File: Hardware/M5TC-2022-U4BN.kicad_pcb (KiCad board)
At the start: 2 copper layers, 127 x 127 mm, 71 parts, among them J1 VCC, J10 SLIDE_DATA_0, J11 SLIDE_DATA_1, J12 SLIDE_DATA_2, J13 SLIDE_DATA_3, J14 ISP, J15 A-G, J2 GND, J3 DATA_0, J4 DATA_1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

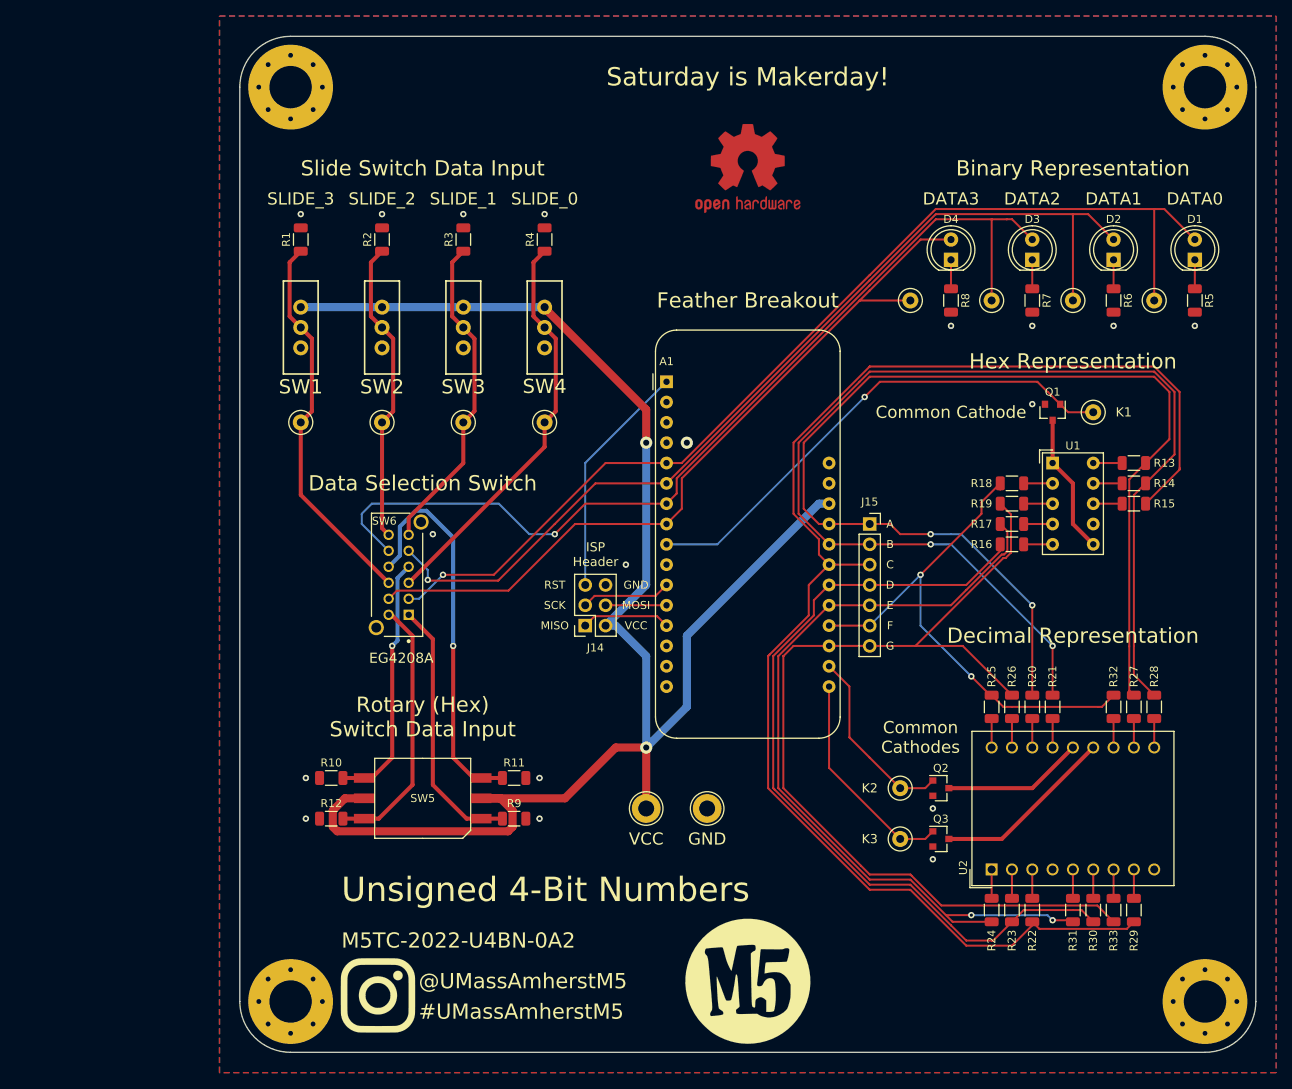
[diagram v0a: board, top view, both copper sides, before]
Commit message: Added triple test points
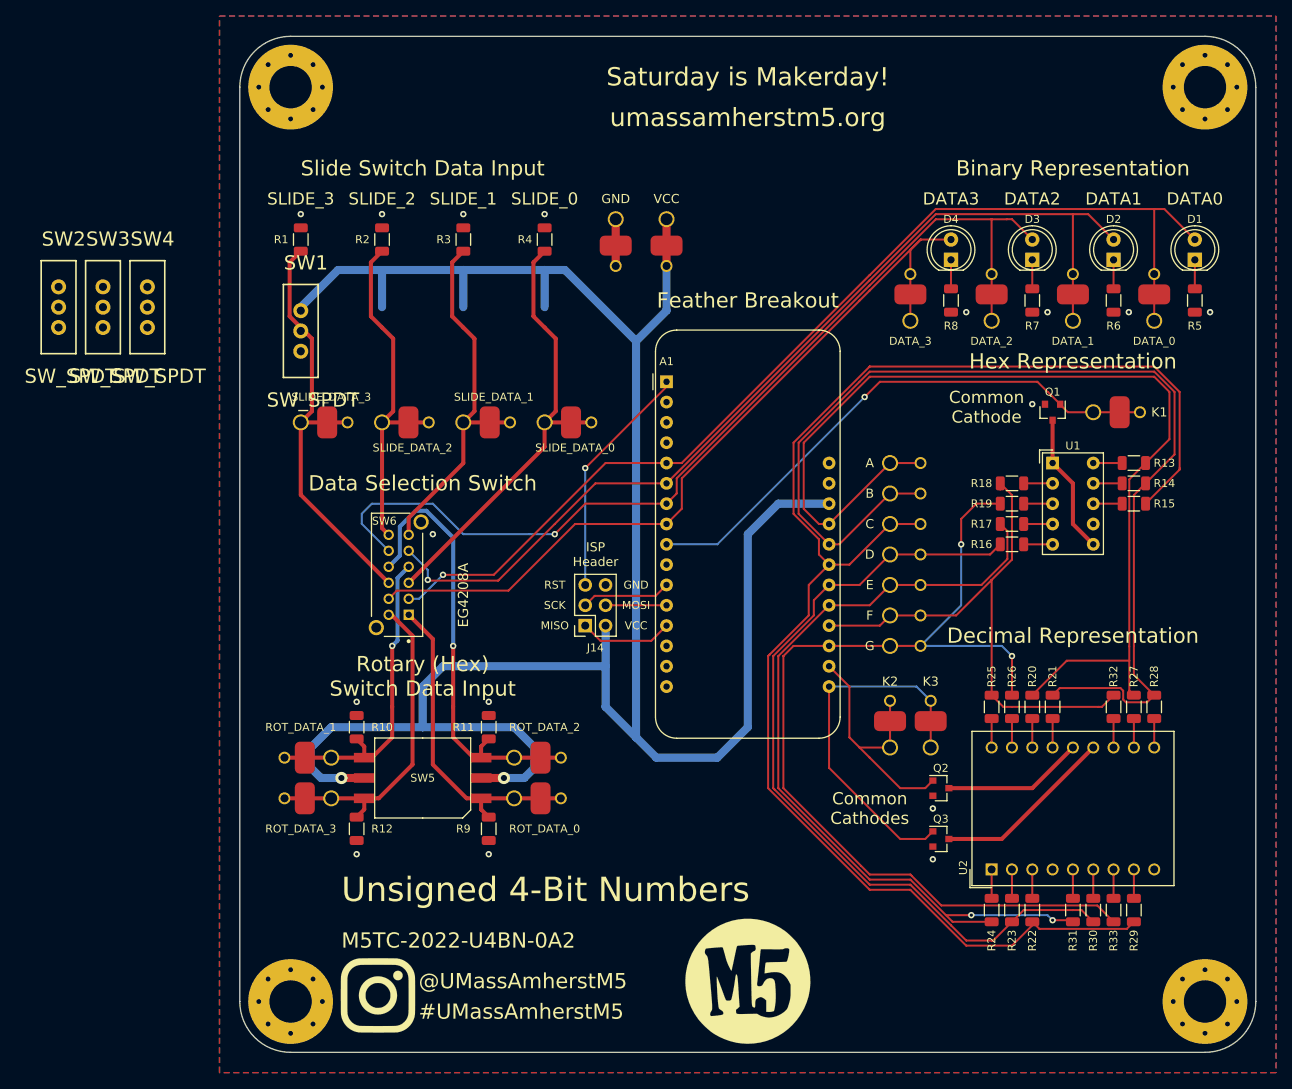
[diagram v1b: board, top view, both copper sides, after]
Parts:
- removed J1: VCC, TestPoint:TestPoint_Loop_D3.80mm_Drill2.0mm
- removed J10: SLIDE_DATA_0, TestPoint:TestPoint_Loop_D2.50mm_Drill1.0mm
- removed J11: SLIDE_DATA_1, TestPoint:TestPoint_Loop_D2.50mm_Drill1.0mm
- removed J12: SLIDE_DATA_2, TestPoint:TestPoint_Loop_D2.50mm_Drill1.0mm
- removed J13: SLIDE_DATA_3, TestPoint:TestPoint_Loop_D2.50mm_Drill1.0mm
- removed J15: A-G, Connector_PinSocket_2.54mm:PinSocket_1x07_P2.54mm_Vertical
- removed J2: GND, TestPoint:TestPoint_Loop_D3.80mm_Drill2.0mm
- removed J3: DATA_0, TestPoint:TestPoint_Loop_D2.50mm_Drill1.0mm
- removed J4: DATA_1, TestPoint:TestPoint_Loop_D2.50mm_Drill1.0mm
- removed J5: DATA_2, TestPoint:TestPoint_Loop_D2.50mm_Drill1.0mm
- removed J6: DATA_3, TestPoint:TestPoint_Loop_D2.50mm_Drill1.0mm
- removed J7: K1, TestPoint:TestPoint_Loop_D2.50mm_Drill1.0mm
- removed J8: K2, TestPoint:TestPoint_Loop_D2.50mm_Drill1.0mm
- removed J9: K3, TestPoint:TestPoint_Loop_D2.50mm_Drill1.0mm
- removed REF**: OSHW-Logo2_14.6x12mm_Copper, Symbol:OSHW-Logo2_14.6x12mm_Copper
- added TP1: VCC, Custom_TestPoint:TestPoint_LoopPostPad, F.Cu at (205.7, 124.5)
- added TP10: Conn_01x01, Custom_TestPoint:TestPoint_LoopPost, F.Cu at (233.7, 166.4)
- added TP11: Conn_01x01, Custom_TestPoint:TestPoint_LoopPost, F.Cu at (233.7, 170.2)
- added TP12: Conn_01x01, Custom_TestPoint:TestPoint_LoopPost, F.Cu at (233.7, 174.0)
- added TP13: Conn_01x01, Custom_TestPoint:TestPoint_LoopPost, F.Cu at (233.7, 177.8)
- added TP14: K1, Custom_TestPoint:TestPoint_LoopPostPad, F.Cu at (259.1, 148.6)
- added TP15: K2, Custom_TestPoint:TestPoint_LoopPostPad, F.Cu at (233.7, 190.5)
- added TP16: K3, Custom_TestPoint:TestPoint_LoopPostPad, F.Cu at (238.8, 190.5)
- added TP17: SLIDE_DATA_0, Custom_TestPoint:TestPoint_LoopPostPad, F.Cu at (190.5, 149.9)
- added TP18: SLIDE_DATA_1, Custom_TestPoint:TestPoint_LoopPostPad, F.Cu at (180.3, 149.9)
- added TP19: SLIDE_DATA_2, Custom_TestPoint:TestPoint_LoopPostPad, F.Cu at (170.2, 149.9)
- added TP2: GND, Custom_TestPoint:TestPoint_LoopPostPad, F.Cu at (199.4, 124.5)
- added TP20: SLIDE_DATA_3, Custom_TestPoint:TestPoint_LoopPostPad, F.Cu at (160.0, 149.9)
- added TP21: ROT_DATA_0, Custom_TestPoint:TestPoint_LoopPostPad, F.Cu at (186.7, 196.8)
- added TP22: ROT_DATA_1, Custom_TestPoint:TestPoint_LoopPostPad, F.Cu at (163.8, 191.8)
- added TP23: ROT_DATA_2, Custom_TestPoint:TestPoint_LoopPostPad, F.Cu at (186.7, 191.8)
- added TP24: ROT_DATA_3, Custom_TestPoint:TestPoint_LoopPostPad, F.Cu at (163.8, 196.8)
- added TP3: DATA_0, Custom_TestPoint:TestPoint_LoopPostPad, F.Cu at (266.7, 137.2)
- added TP4: DATA_1, Custom_TestPoint:TestPoint_LoopPostPad, F.Cu at (256.5, 137.2)
- added TP5: DATA_2, Custom_TestPoint:TestPoint_LoopPostPad, F.Cu at (246.4, 137.2)
- added TP6: DATA_3, Custom_TestPoint:TestPoint_LoopPostPad, F.Cu at (236.2, 137.2)
- added TP7: Conn_01x01, Custom_TestPoint:TestPoint_LoopPost, F.Cu at (233.7, 154.9)
- added TP8: Conn_01x01, Custom_TestPoint:TestPoint_LoopPost, F.Cu at (233.7, 158.8)
- added TP9: Conn_01x01, Custom_TestPoint:TestPoint_LoopPost, F.Cu at (233.7, 162.6)
- moved SW4 49.7 mm to (140.8, 135.5)
- moved SW3 45.1 mm to (135.3, 135.5)
- moved SW2 40.5 mm to (129.7, 135.5)
- moved R11 7.10 mm to (183.5, 188.0), turned to 90 degrees
- moved R10 7.10 mm to (167.0, 188.0), turned to 270 degrees
- moved R9 3.42 mm to (183.5, 200.7), turned to 90 degrees
- moved R12 3.42 mm to (167.0, 200.7), turned to 90 degrees
- moved SW5 2.54 mm to (175.3, 194.3)
- moved SW1 0.43 mm to (160.0, 138.4)
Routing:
- net VCC: track 203.5 -> 274.3 mm
- net K3: track 27.2 -> 46.5 mm
- net A: track 143.2 -> 130.9 mm, vias 2 -> 0
- net B: track 146.4 -> 135.9 mm, vias 2 -> 0
- net K2: track 23.4 -> 33.0 mm
- net C: track 178.6 -> 187.1 mm
- net ROT_DATA_2: track 49.2 -> 56.7 mm
- net ROT_DATA_0: track 33.0 -> 40.5 mm
- net ROT_DATA_1: track 31.9 -> 39.4 mm
- net ROT_DATA_3: track 33.1 -> 40.7 mm
- net K1: track 63.3 -> 69.2 mm
- net SLIDE_DATA_0: track 50.8 -> 56.6 mm
- net GND: track 0.00 -> 5.84 mm, vias 18 -> 16
- net SLIDE_DATA_3: track 48.3 -> 54.2 mm
- net SLIDE_DATA_2: track 38.1 -> 43.9 mm
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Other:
- board text added: "DATA_0"
- board text added: "DATA_1"
- board text added: "DATA_2"
- board text added: "DATA_3"
- board text added: "ROT_DATA_0"
- board text added: "ROT_DATA_1"
- board text added: "ROT_DATA_2"
- board text added: "ROT_DATA_3"
- board text added: "SLIDE_DATA_0"
- board text added: "SLIDE_DATA_1"
- board text added: "SLIDE_DATA_2"
- board text added: "SLIDE_DATA_3"

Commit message: Rerouted Board, Changed SOIC-Hex Size
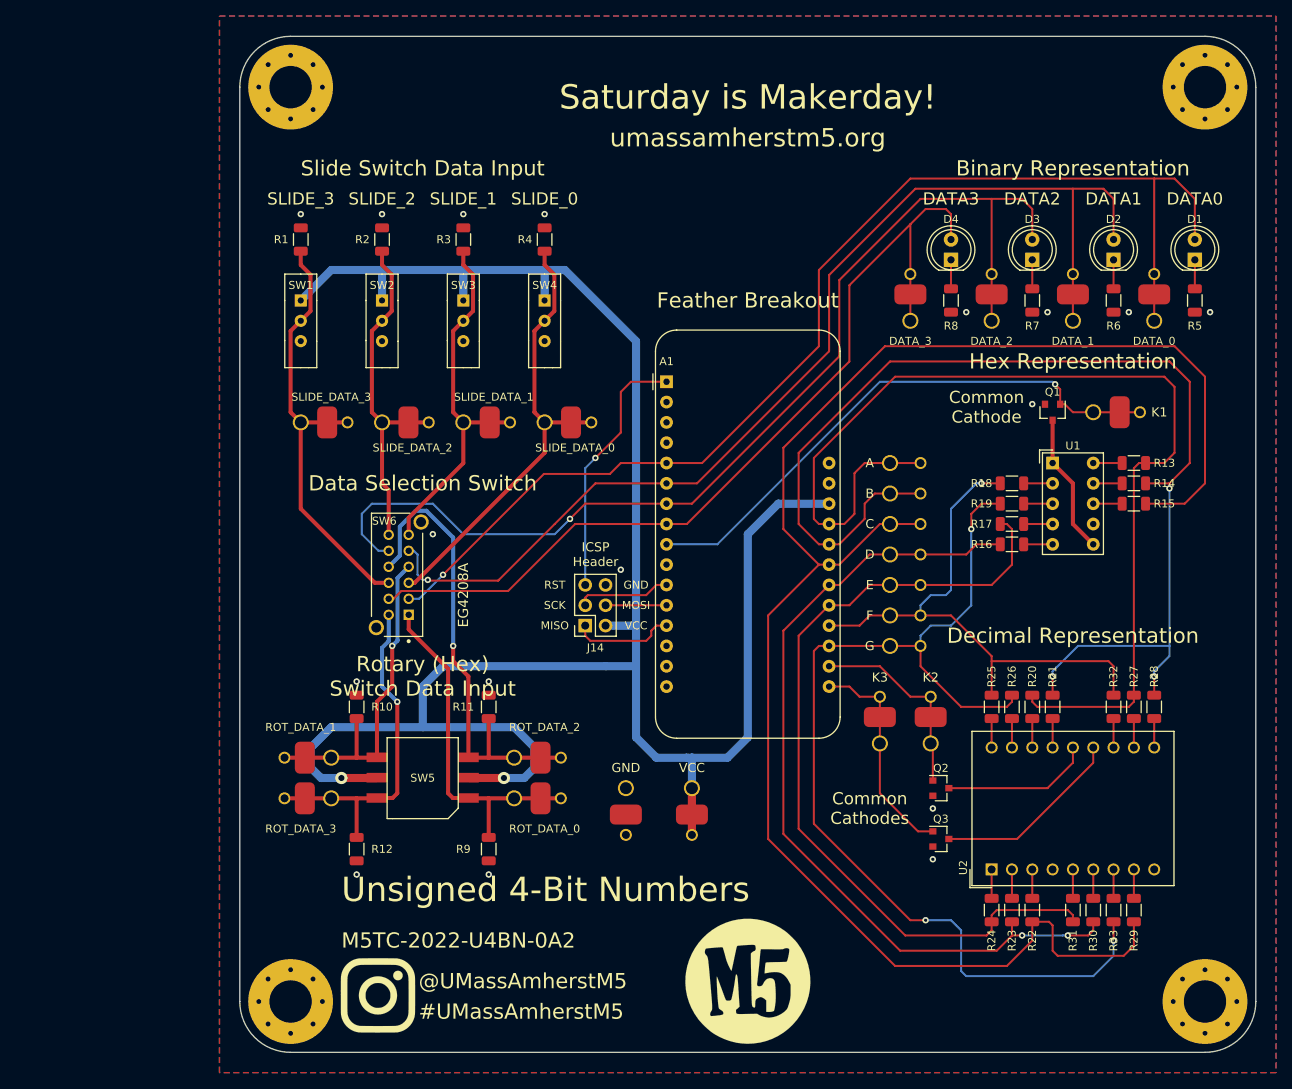
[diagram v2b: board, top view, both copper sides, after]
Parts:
- SW1, SW2, SW3, SW4: footprint SparkFun-Electromechanical:SWITCH-SPDT -> 4PDT_Footprint:E-Switch-EG1218
- moved TP1 71.2 mm to (208.9, 195.6)
- moved TP2 71.1 mm to (200.7, 195.6)
- moved SW4 49.7 mm to (190.5, 134.6)
- moved SW3 45.1 mm to (180.3, 134.6)
- moved SW2 40.4 mm to (170.2, 134.6)
- moved TP16 6.37 mm to (232.4, 190.0)
- moved TP15 5.11 mm to (238.8, 190.0)
- moved SW1 3.81 mm to (160.0, 134.6)
- moved R10 2.54 mm to (167.0, 185.4)
- moved R11 2.54 mm to (183.5, 185.4)
- moved R12 2.54 mm to (167.0, 203.2)
- moved R9 2.54 mm to (183.5, 203.2)
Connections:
- A1 pad 10: Net-(A1-Pad10) -> unconnected-(A1-Pad10)
- A1 pad 14: Net-(A1-Pad14) -> unconnected-(A1-Pad14)
- A1 pad 15: Net-(A1-Pad15) -> unconnected-(A1-Pad15)
- A1 pad 16: Net-(A1-Pad16) -> unconnected-(A1-Pad16)
- A1 pad 2: Net-(A1-Pad2) -> unconnected-(A1-Pad2)
- A1 pad 27: Net-(A1-Pad27) -> unconnected-(A1-Pad27)
- A1 pad 28: Net-(A1-Pad28) -> unconnected-(A1-Pad28)
- A1 pad 3: Net-(A1-Pad3) -> unconnected-(A1-Pad3)
- SW1 pad 3: Net-(SW1-Pad3) -> unconnected-(SW1-Pad3)
- SW2 pad 3: Net-(SW2-Pad3) -> unconnected-(SW2-Pad3)
- SW3 pad 3: Net-(SW3-Pad3) -> unconnected-(SW3-Pad3)
- SW4 pad 3: Net-(SW4-Pad3) -> unconnected-(SW4-Pad3)
- U1 pad 7: Net-(U1-Pad7) -> unconnected-(U1-Pad7)
- U2 pad 4: Net-(U2-Pad4) -> unconnected-(U2-Pad4)
- U2 pad 9: Net-(U2-Pad9) -> unconnected-(U2-Pad9)
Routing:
- net C: track 187.1 -> 212.6 mm
- net K3: track 46.5 -> 27.5 mm
- net DATA_0: track 134.0 -> 149.5 mm
- net DATA_1: track 124.0 -> 139.1 mm
- net VCC: track 274.3 -> 260.3 mm
- net DATA_2: track 123.1 -> 135.2 mm
- net B: track 135.9 -> 146.5 mm, vias 0 -> 3
- net DATA_3: track 101.8 -> 111.6 mm
- net K2: track 33.0 -> 24.9 mm
- net G: track 122.9 -> 130.8 mm, vias 2 -> 3
- net GND: track 5.84 -> 0.00 mm, vias 16 -> 17
- net D: track 101.9 -> 105.6 mm, vias 0 -> 2
- net A: track 130.9 -> 134.6 mm
- net RST: track 29.6 -> 32.8 mm
- net ROT_DATA_0: track 40.5 -> 43.6 mm
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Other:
- outline, holes or cut-outs redrawn
- net class Default removed
- board text added: "ICSP Header"
- board text removed: "ISP Header"

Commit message: Updated software to clear segments
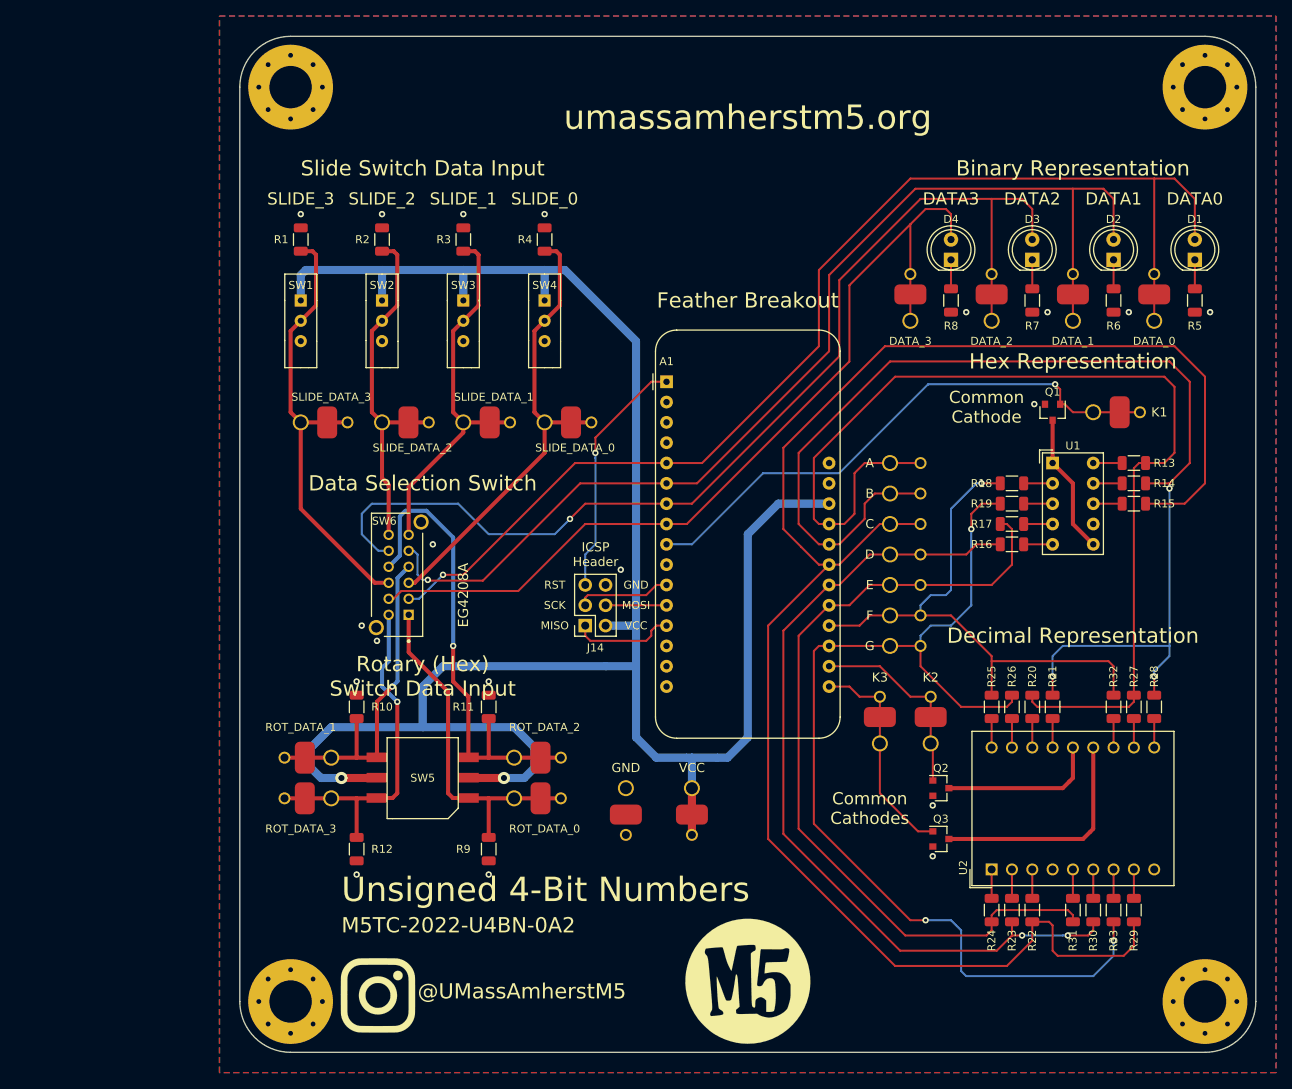
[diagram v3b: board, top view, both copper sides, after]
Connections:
- net Net-(Q1-Pad3) renamed DIG1
- net Net-(Q2-Pad3) renamed DIG2
- net Net-(Q3-Pad3) renamed DIG3
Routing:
- net DIG3: track 23.9 -> 28.7 mm
- net RST: track 32.8 -> 30.7 mm
- net VCC: track 260.3 -> 262.2 mm
- net SLIDE_DATA_2: track 43.7 -> 45.1 mm
- net SLIDE_DATA_3: track 54.9 -> 56.3 mm
- net SLIDE_DATA_1: track 46.2 -> 47.6 mm
- net SLIDE_DATA_0: track 56.8 -> 58.3 mm
- net B: track 146.5 -> 147.6 mm
- net DIG2: track 18.7 -> 19.8 mm
- net ROT_DATA_2: track 59.3 -> 60.0 mm
- net C: track 212.6 -> 213.1 mm
- net GND: vias 17 -> 19
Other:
- board text added: "Designers: Akshat Sahay - CE 2023, Chris Caron - MS EE 2023, Samridh Tuteja - CE 2024"
- board text removed: "#UMassAmherstM5"
- board text removed: "Designers: Akshat Sahay - CE 2023, Chris Caron - MS EE 2023"
- board text removed: "Saturday is Makerday!"
